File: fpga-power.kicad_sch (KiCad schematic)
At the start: 73 parts, among them U3 XC7K70T-FBG484

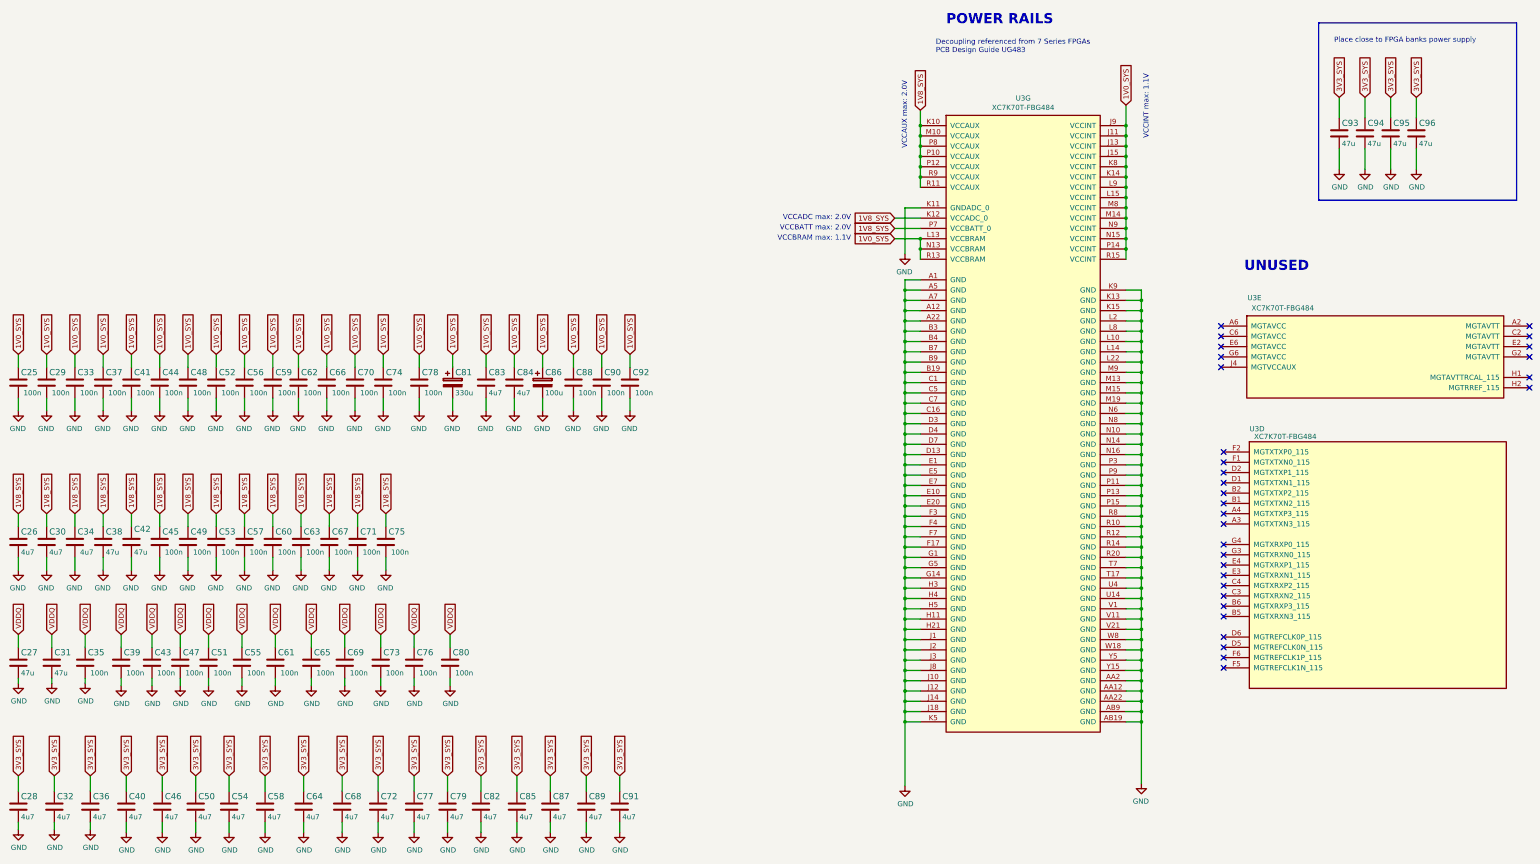
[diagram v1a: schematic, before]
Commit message: Introduce standardized components
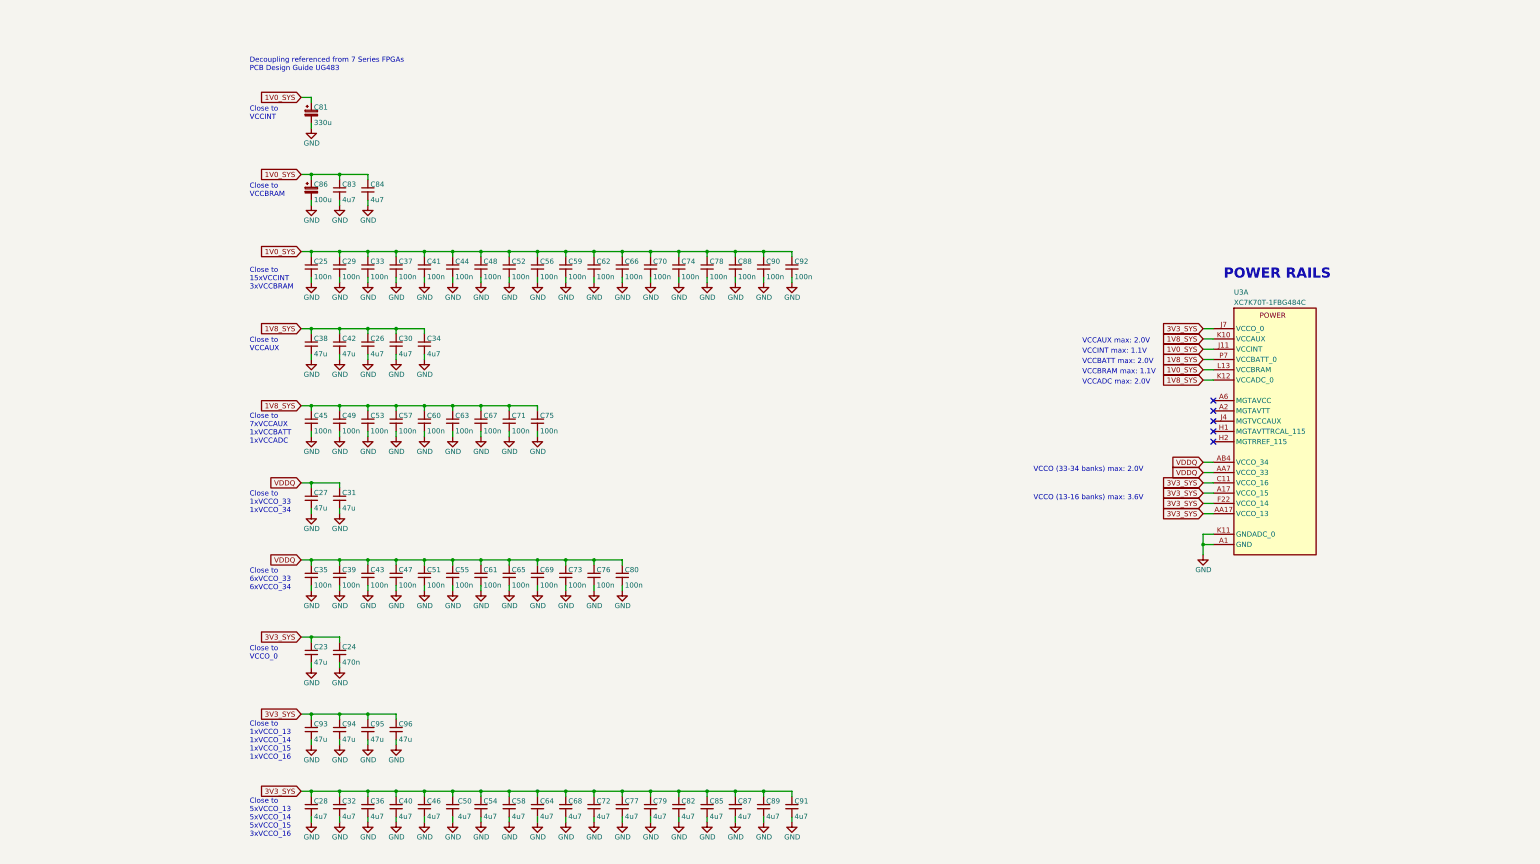
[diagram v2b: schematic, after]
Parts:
- removed U3: XC7K70T-FBG484, lpddr4-test-board-footprints:BGA484C100P22X22_2300X2300X244N, symbol lpddr4-test-board:XC7K70T-FBG484
- added C23: C_47u_0603, lpddr4-test-board-footprints:C_0603_1608Metric, symbol lpddr4-test-board:C_47u_0603
- added C24: C_470n_0402, lpddr4-test-board-footprints:C_0402_1005Metric, symbol lpddr4-test-board:C_470n_0402
- added U3: XC7K70T-FBG484, lpddr4-test-board-footprints:BGA484C100P22X22_2300X2300X244N, symbol lpddr4-test-board:XC7K70T-FBG484
- C25, C29, C33, C35, C37, C39, C41, C43, C44, C45, C47, C48, C49, C51, C52, C53, C55, C56, C57, C59, C60, C61, C62, C63, C65, C66, C67, C69, C70, C71, C73, C74, C75, C76, C78, C80, C88, C90, C92: footprint lpddr4-test-board-footprints:0201-res -> lpddr4-test-board-footprints:C_0201; Author (none) -> Antmicro; License (none) -> Apache-2.0; Manufacturer YAGEO -> Yaego
- C26, C28, C30, C32, C34, C36, C40, C46, C50, C54, C58, C64, C68, C72, C77, C79, C82, C83, C84, C85, C87, C89, C91: footprint lpddr4-test-board-footprints:0402-cap -> lpddr4-test-board-footprints:C_0402_1005Metric; Author (none) -> Antmicro; License (none) -> Apache-2.0; Manufacturer MURATA -> Murata
- C27, C31, C38, C42, C93, C94, C95, C96: footprint lpddr4-test-board-footprints:0603-cap -> lpddr4-test-board-footprints:C_0603_1608Metric; Author (none) -> Antmicro; License (none) -> Apache-2.0; Manufacturer MURATA -> Murata
- C81: Author (none) -> Antmicro; License (none) -> Apache-2.0
- C86: Author (none) -> Antmicro; License (none) -> Apache-2.0; Manufacturer VISHAY -> Vishay
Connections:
- net 1V0_SYS: now also U3.J11 (VCCINT), U3.J13 (VCCINT), U3.J15 (VCCINT), U3.J9 (VCCINT), U3.K14 (VCCINT), U3.K8 (VCCINT), U3.L13 (VCCBRAM), U3.L15 (VCCINT), U3.L9 (VCCINT), U3.M14 (VCCINT), U3.M8 (VCCINT), U3.N13 (VCCBRAM), U3.N15 (VCCINT), U3.N9 (VCCINT), U3.P14 (VCCINT), U3.R13 (VCCBRAM), U3.R15 (VCCINT)
- net 1V8_SYS: now also U3.K10 (VCCAUX), U3.K12 (VCCADC_0), U3.M10 (VCCAUX), U3.P10 (VCCAUX), U3.P12 (VCCAUX), U3.P7 (VCCBATT_0), U3.P8 (VCCAUX), U3.R11 (VCCAUX), U3.R9 (VCCAUX)
- net 3V3_SYS: now also C23.1, C24.1, U3.A17 (VCCO_15), U3.AA17 (VCCO_13), U3.AB14 (VCCO_13), U3.B14 (VCCO_15), U3.C11 (VCCO_16), U3.C21 (VCCO_15), U3.D18 (VCCO_15), U3.D8 (VCCO_16), U3.E15 (VCCO_15), U3.F12 (VCCO_16), U3.F22 (VCCO_14), U3.G19 (VCCO_14), U3.G9 (VCCO_16), U3.H16 (VCCO_15), U3.J7 (VCCO_0), U3.K20 (VCCO_14), U3.L17 (VCCO_14), U3.N21 (VCCO_14), U3.N7 (VCCO_0), U3.P18 (VCCO_14), U3.T22 (VCCO_13), U3.U19 (VCCO_13), U3.V16 (VCCO_13), U3.Y20 (VCCO_13)
- net GND: now also C23.2, C24.2, U3.A1 (GND), U3.A12 (GND), U3.A22 (GND), U3.A5 (GND), U3.A7 (GND), U3.AA12 (GND), U3.AA2 (GND), U3.AA22 (GND), U3.AB19 (GND), U3.AB9 (GND), U3.B19 (GND), U3.B3 (GND), U3.B4 (GND), U3.B7 (GND), U3.B9 (GND), U3.C1 (GND), U3.C16 (GND), U3.C5 (GND), U3.C7 (GND), U3.D13 (GND), U3.D3 (GND), U3.D4 (GND), U3.D7 (GND), U3.E1 (GND), U3.E10 (GND), U3.E20 (GND), U3.E5 (GND), U3.E7 (GND), U3.F17 (GND), U3.F3 (GND), U3.F4 (GND), U3.F7 (GND), U3.G1 (GND), U3.G14 (GND), U3.G5 (GND), U3.H11 (GND), U3.H21 (GND), U3.H3 (GND), U3.H4 (GND), U3.H5 (GND), U3.J1 (GND), U3.J10 (GND), U3.J12 (GND), U3.J14 (GND), U3.J18 (GND), U3.J2 (GND), U3.J3 (GND), U3.J8 (GND), U3.K11 (GNDADC_0), U3.K13 (GND), U3.K15 (GND), U3.K5 (GND), U3.K9 (GND), U3.L10 (GND), U3.L14 (GND), U3.L2 (GND), U3.L22 (GND), U3.L8 (GND), U3.M13 (GND), U3.M15 (GND), U3.M19 (GND), U3.M9 (GND), U3.N10 (GND), U3.N14 (GND), U3.N16 (GND), U3.N6 (GND), U3.N8 (GND), U3.P11 (GND), U3.P13 (GND), U3.P15 (GND), U3.P3 (GND), U3.P9 (GND), U3.R10 (GND), U3.R12 (GND), U3.R14 (GND), U3.R20 (GND), U3.R8 (GND), U3.T17 (GND), U3.T7 (GND), U3.U14 (GND), U3.U4 (GND), U3.V1 (GND), U3.V11 (GND), U3.V21 (GND), U3.W18 (GND), U3.W8 (GND), U3.Y15 (GND), U3.Y5 (GND)
- net VDDQ: now also U3.AA7 (VCCO_33), U3.AB4 (VCCO_34), U3.M4 (VCCO_34), U3.N1 (VCCO_34), U3.R5 (VCCO_34), U3.T12 (VCCO_33), U3.T2 (VCCO_34), U3.U9 (VCCO_33), U3.V6 (VCCO_33), U3.W13 (VCCO_33), U3.W3 (VCCO_34), U3.Y10 (VCCO_33)
- new net: U3.A2 (MGTAVTT), U3.C2 (MGTAVTT), U3.E2 (MGTAVTT), U3.G2 (MGTAVTT)
- new net: U3.A6 (MGTAVCC), U3.C6 (MGTAVCC), U3.E6 (MGTAVCC), U3.G6 (MGTAVCC)
- no-connect marks 31 -> 5
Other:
- note added: "Close to 15xVCCINT 3xVCCBRAM"
- note added: "Close to 1xVCCO_13 1xVCCO_14 1xVCCO_15 1xVCCO_16"
- note added: "Close to 1xVCCO_33 1xVCCO_34"
- note added: "Close to 5xVCCO_13 5xVCCO_14 5xVCCO_15 3xVCCO_16"
- note added: "Close to 6xVCCO_33 6xVCCO_34"
- note added: "Close to 7xVCCAUX 1xVCCBATT 1xVCCADC"
- note added: "Close to VCCAUX"
- note added: "Close to VCCBRAM"
- note added: "Close to VCCINT"
- note added: "Close to VCCO_0"
- note added: "VCCO (13-16 banks) max: 3.6V"
- note added: "VCCO (33-34 banks) max: 2.0V"
- note removed: "Place close to FPGA banks power supply"
- note removed: "UNUSED"
- moved on the sheet: C25, C26, C27, C28, C29, C30, C31, C32, C33, C34, C35, C36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

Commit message: [#55158] components update
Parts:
- U3: Manufacturer Xilinx -> AMD-Xilinx
